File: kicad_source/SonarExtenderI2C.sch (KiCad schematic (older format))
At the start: 50 parts, among them CN2 CONN_01X04, CN3 CONN_01X04, CN4 CONN_01X04, CN5 CONN_01X04, CN6 CONN_01X04, P1 CONN_01X06, U1 NE555-IC_logic, U10 74xx590-IC_logic, U11 74xx590-IC_logic, U12 74xx590-IC_logic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

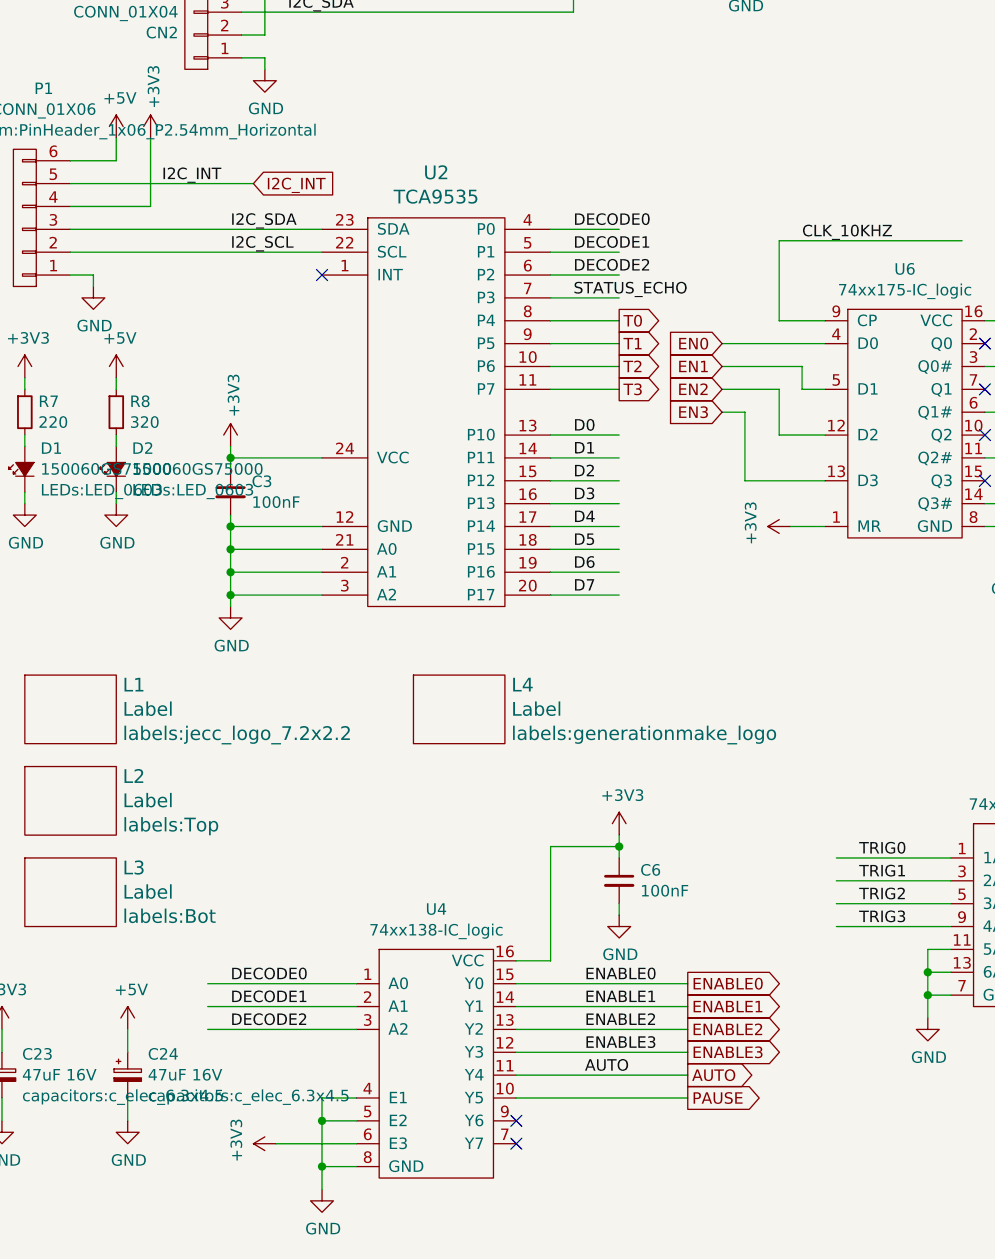
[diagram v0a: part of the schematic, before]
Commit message: updated schematics
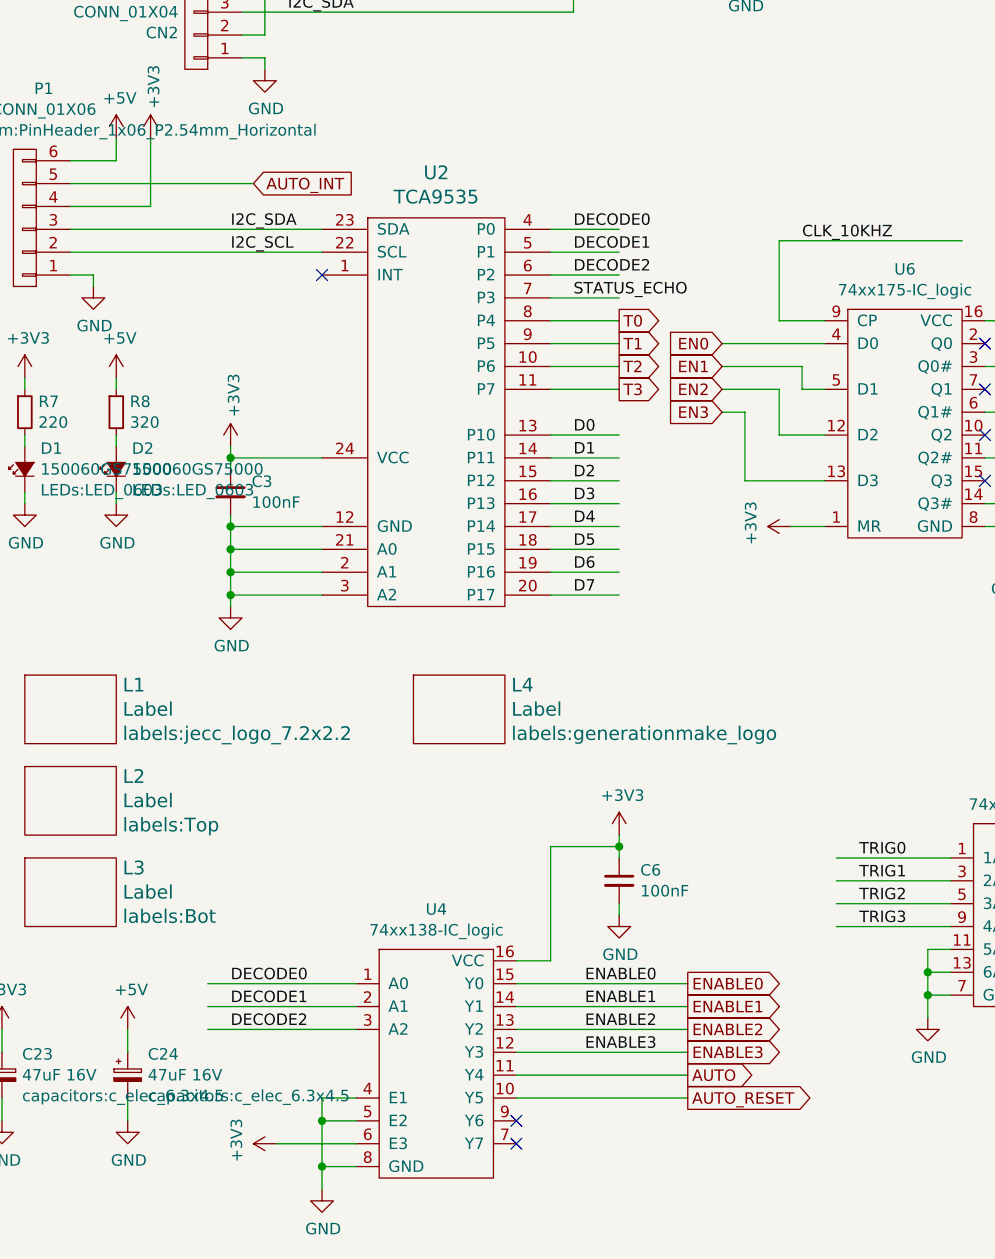
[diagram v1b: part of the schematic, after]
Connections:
- net labels added: AUTO_INT, AUTO_RESET
- net labels removed: I2C_INT, PAUSE
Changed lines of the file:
@@
 Wire Wire Line
 	2950 7100 3700 7100
-Text Label 3250 7100 0    50   ~ 0
-AUTO
 Text GLabel 3700 6700 2    50   Output ~ 0
 ENABLE0
@@
 Text GLabel 3700 7000 2    50   Output ~ 0
 ENABLE3
-Text GLabel 3700 7100 2    50   Output ~ 0
-AUTO
 $Sheet
 S 5300 7250 1250 400
@@
 Wire Wire Line
 	1800 3200 1000 3200
-Text Label 1400 3200 0    50   ~ 0
-I2C_INT
 Text GLabel 1800 3200 2    50   Input ~ 0
-I2C_INT
+AUTO_INT
 $Comp
 L mechanical-connectors:CONN_01X04 CN2
@@
 	2950 7200 3700 7200
 Text GLabel 3700 7200 2    50   Output ~ 0
-PAUSE
+AUTO_RESET
+Text GLabel 3700 7100 2    50   Output ~ 0
+AUTO
 $EndSCHEMATC

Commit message: solved issues in schematics
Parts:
- added JP? (x3): Jumper_NC_Small, wire_pads:SolderJumper_2mm, symbol devices:Jumper_NC_Small
- added R? (x3): 10k, resistors:R_0603, symbol devices:R_0603
- R7: value 220 -> 1k
- R8: value 320 -> 1k
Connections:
- net labels added: A0, A1, A2
- wire segments 344 -> 366
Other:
- moved on the sheet: C9, U7

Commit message: updated schematics pdf
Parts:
- U1: symbol SonarExtenderI2C-rescue:NE555-IC_logic -> SonarExtenderI2C-rescue:NE555-IC_logic-SonarExtenderI2C-rescue-SonarExtenderI2C-rescue
- U10, U11, U12, U9: symbol SonarExtenderI2C-rescue:74xx590-IC_logic -> SonarExtenderI2C-rescue:74xx590-IC_logic-SonarExtenderI2C-rescue-SonarExtenderI2C-rescue-SonarExtenderI2C-rescue
- U13: symbol SonarExtenderI2C-rescue:74xx4002-IC_logic -> SonarExtenderI2C-rescue:74xx4002-IC_logic-SonarExtenderI2C-rescue-SonarExtenderI2C-rescue
- U2: symbol SonarExtenderI2C-rescue:TCA9535-IC_interface_i2c -> SonarExtenderI2C-rescue:TCA9535-IC_interface_i2c-SonarExtenderI2C-rescue-SonarExtenderI2C-rescue
- U4: symbol SonarExtenderI2C-rescue:74xx138-IC_logic -> SonarExtenderI2C-rescue:74xx138-IC_logic-SonarExtenderI2C-rescue-SonarExtenderI2C-rescue-SonarExtenderI2C-rescue
- U6: symbol SonarExtenderI2C-rescue:74xx175-IC_logic -> SonarExtenderI2C-rescue:74xx175-IC_logic-SonarExtenderI2C-rescue-SonarExtenderI2C-rescue
- U7: symbol SonarExtenderI2C-rescue:74xx04-IC_logic -> SonarExtenderI2C-rescue:74xx04-IC_logic-SonarExtenderI2C-rescue-SonarExtenderI2C-rescue
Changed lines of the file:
@@
 $EndComp
 $Comp
-L SonarExtenderI2C-rescue:74xx590-IC_logic U12
+L SonarExtenderI2C-rescue:74xx590-IC_logic-SonarExtenderI2C-rescue-SonarExtenderI2C-rescue-SonarExtenderI2C-rescue U12
 U 1 1 5EE73281
 P 8200 6150
@@
 $EndComp
 $Comp
-L SonarExtenderI2C-rescue:74xx590-IC_logic U11
+L SonarExtenderI2C-rescue:74xx590-IC_logic-SonarExtenderI2C-rescue-SonarExtenderI2C-rescue-SonarExtenderI2C-rescue U11
 U 1 1 5EE73231
 P 8200 4650
@@
 $EndComp
 $Comp
-L SonarExtenderI2C-rescue:74xx590-IC_logic U10
+L SonarExtenderI2C-rescue:74xx590-IC_logic-SonarExtenderI2C-rescue-SonarExtenderI2C-rescue-SonarExtenderI2C-rescue U10
 U 1 1 5EE4DE46
 P 8200 3000
@@
 $EndComp
 $Comp
-L SonarExtenderI2C-rescue:74xx590-IC_logic U9
+L SonarExtenderI2C-rescue:74xx590-IC_logic-SonarExtenderI2C-rescue-SonarExtenderI2C-rescue-SonarExtenderI2C-rescue U9
 U 1 1 5ED3FBEA
 P 8200 1500
@@
 $EndComp
 $Comp
-L SonarExtenderI2C-rescue:74xx04-IC_logic U7
+L SonarExtenderI2C-rescue:74xx04-IC_logic-SonarExtenderI2C-rescue-SonarExtenderI2C-rescue U7
 U 1 1 5EEE08C7
 P 5050 6850
@@
 $EndComp
 $Comp
-L SonarExtenderI2C-rescue:74xx138-IC_logic U4
+L SonarExtenderI2C-rescue:74xx138-IC_logic-SonarExtenderI2C-rescue-SonarExtenderI2C-rescue-SonarExtenderI2C-rescue U4
 U 1 1 5F07A383
 P 2600 7050
@@
 $EndComp
 $Comp
-L SonarExtenderI2C-rescue:TCA9535-IC_interface_i2c U2
+L SonarExtenderI2C-rescue:TCA9535-IC_interface_i2c-SonarExtenderI2C-rescue-SonarExtenderI2C-rescue U2
 U 1 1 5F072FE1
 P 2600 4300
@@
 $EndComp
 $Comp
-L SonarExtenderI2C-rescue:74xx175-IC_logic U6
+L SonarExtenderI2C-rescue:74xx175-IC_logic-SonarExtenderI2C-rescue-SonarExtenderI2C-rescue U6
 U 1 1 5ED68086
 P 4650 4250
@@
 $EndComp
 $Comp
-L SonarExtenderI2C-rescue:NE555-IC_logic U1
+L SonarExtenderI2C-rescue:NE555-IC_logic-SonarExtenderI2C-rescue-SonarExtenderI2C-rescue U1
 U 1 1 5ED3F84C
 P 1950 1400
@@
 $EndComp
 $Comp
-L SonarExtenderI2C-rescue:74xx4002-IC_logic U13
+L SonarExtenderI2C-rescue:74xx4002-IC_logic-SonarExtenderI2C-rescue-SonarExtenderI2C-rescue U13
 U 1 1 5EF9FE5E
 P 10000 5650
